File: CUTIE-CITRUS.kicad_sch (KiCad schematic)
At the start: 0 parts

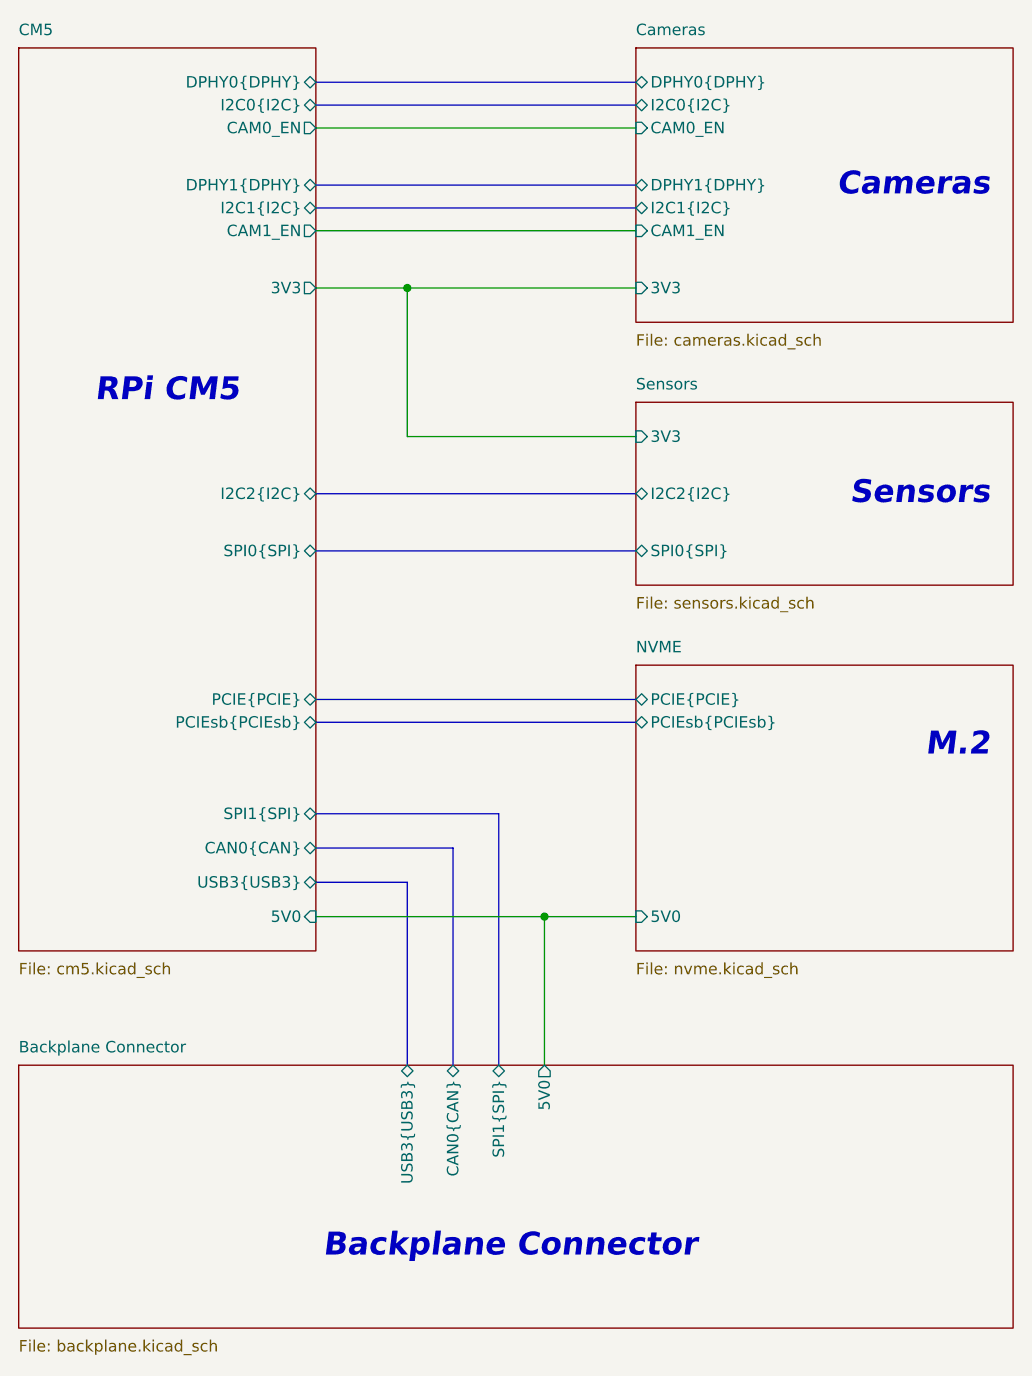
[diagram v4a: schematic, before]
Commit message: removed ublox
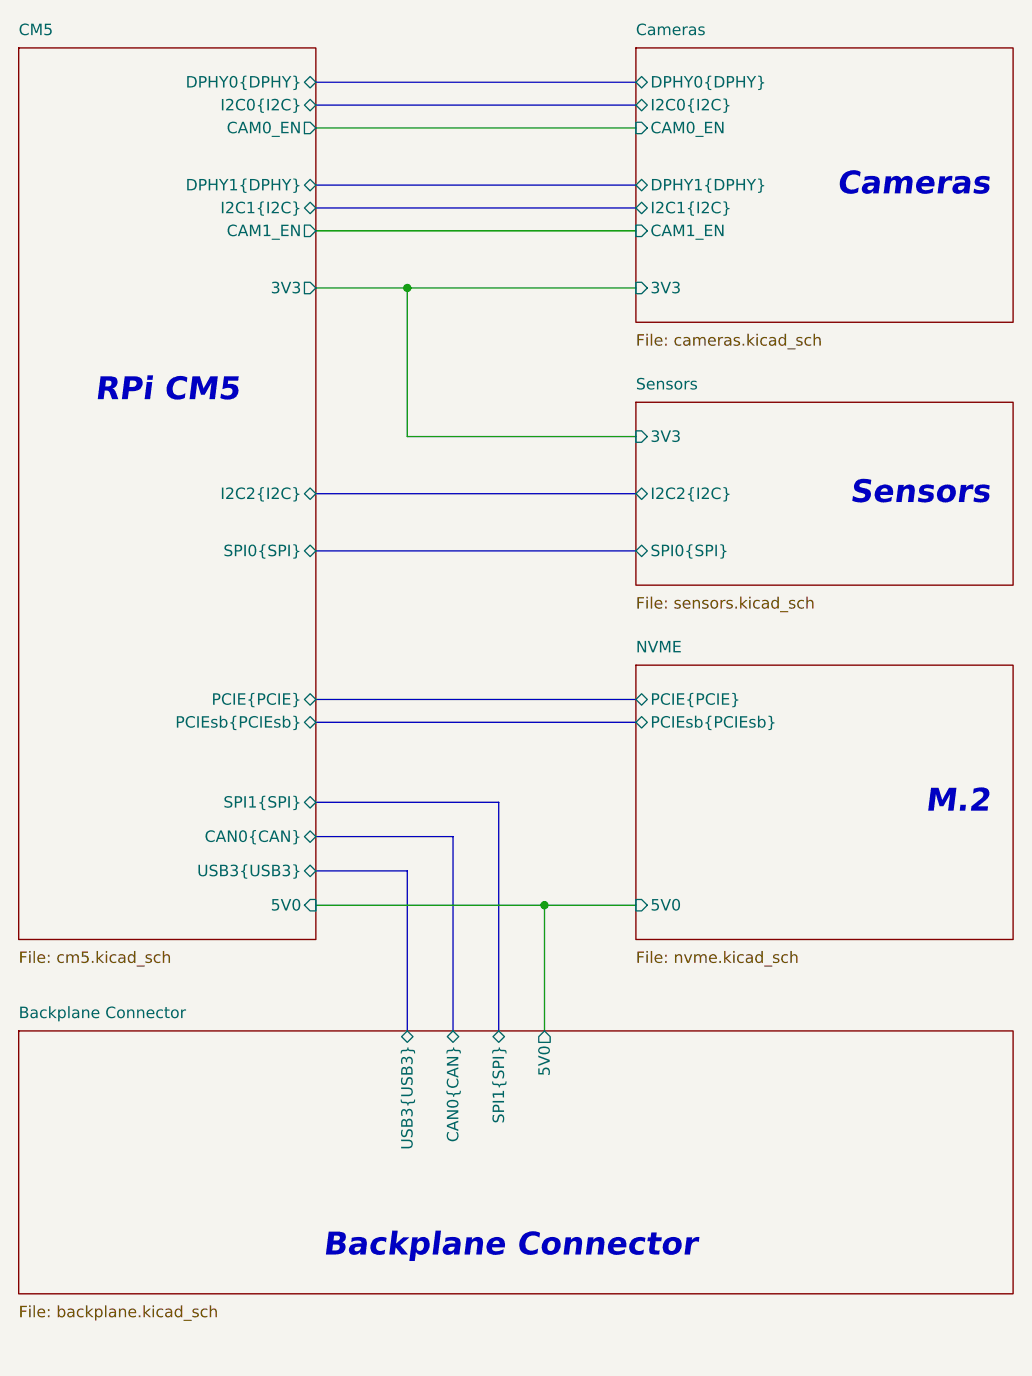
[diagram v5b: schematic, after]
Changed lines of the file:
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@@
 	(text "M.2"
 		(exclude_from_sim no)
-		(at 153.67 113.03 0)
+		(at 153.67 119.38 0)
 		(effects
 			(font
@@
 	)
 	(junction
-		(at 104.14 132.08)
+		(at 104.14 130.81)
 		(diameter 0)
 		(color 255 0 0 1)
@@
 	(wire
 		(pts
-			(xy 104.14 132.08) (xy 114.3 132.08)
+			(xy 104.14 130.81) (xy 114.3 130.81)
 		)
 		(stroke
@@
 	(bus
 		(pts
-			(xy 88.9 128.27) (xy 88.9 148.59)
-		)
-		(stroke
-			(width 0)
-			(type default)
-		)
-	)
-	(wire
-		(pts
-			(xy 104.14 132.08) (xy 104.14 148.59)
+			(xy 88.9 127) (xy 88.9 144.78)
+		)
+		(stroke
+			(width 0)
+			(type default)
+		)
+	)
+	(wire
+		(pts
+			(xy 104.14 130.81) (xy 104.14 144.78)
 		)
 		(stroke
@@
 	(bus
 		(pts
-			(xy 99.06 148.59) (xy 99.06 120.65)
+			(xy 99.06 144.78) (xy 99.06 119.38)
 		)
 		(stroke
@@
 	(bus
 		(pts
-			(xy 99.06 120.65) (xy 78.74 120.65)
+			(xy 99.06 119.38) (xy 78.74 119.38)
 		)
 		(stroke
@@
 	(wire
 		(pts
-			(xy 78.74 132.08) (xy 104.14 132.08)
+			(xy 78.74 44.45) (xy 114.3 44.45)
+		)
+		(stroke
+			(width 0)
+			(type default)
+		)
+	)
+	(wire
+		(pts
+			(xy 78.74 62.23) (xy 88.9 62.23)
+		)
+		(stroke
+			(width 0.381)
+			(type default)
+			(color 255 153 0 1)
+		)
+	)
+	(wire
+		(pts
+			(xy 88.9 62.23) (xy 114.3 62.23)
+		)
+		(stroke
+			(width 0.381)
+			(type default)
+			(color 255 153 0 1)
+		)
+	)
+	(bus
+		(pts
+			(xy 78.74 110.49) (xy 114.3 110.49)
+		)
+		(stroke
+			(width 0)
+			(type default)
+		)
+	)
+	(bus
+		(pts
+			(xy 78.74 41.91) (xy 114.3 41.91)
+		)
+		(stroke
+			(width 0)
+			(type default)
+		)
+	)
+	(bus
+		(pts
+			(xy 93.98 144.78) (xy 93.98 123.19)
+		)
+		(stroke
+			(width 0)
+			(type default)
+		)
+	)
+	(wire
+		(pts
+			(xy 78.74 55.88) (xy 114.3 55.88)
+		)
+		(stroke
+			(width 0)
+			(type default)
+		)
+	)
+	(wire
+		(pts
+			(xy 78.74 130.81) (xy 104.14 130.81)
 		)
 		(stroke
@@
 		)
 	)
-	(wire
-		(pts
-			(xy 78.74 44.45) (xy 114.3 44.45)
-		)
-		(stroke
-			(width 0)
-			(type default)
-		)
-	)
-	(wire
-		(pts
-			(xy 78.74 62.23) (xy 88.9 62.23)
+	(bus
+		(pts
+			(xy 78.74 50.8) (xy 114.3 50.8)
+		)
+		(stroke
+			(width 0)
+			(type default)
+		)
+	)
+	(wire
+		(pts
+			(xy 88.9 62.23) (xy 88.9 78.74)
 		)
 		(stroke
@@
 		)
 	)
-	(wire
-		(pts
-			(xy 88.9 62.23) (xy 114.3 62.23)
-		)
-		(stroke
-			(width 0.381)
-			(type default)
-			(color 255 153 0 1)
-		)
-	)
-	(bus
-		(pts
-			(xy 78.74 110.49) (xy 114.3 110.49)
-		)
-		(stroke
-			(width 0)
-			(type default)
-		)
-	)
-	(bus
-		(pts
-			(xy 78.74 41.91) (xy 114.3 41.91)
-		)
-		(stroke
-			(width 0)
-			(type default)
-		)
-	)
-	(bus
-		(pts
-			(xy 93.98 148.59) (xy 93.98 124.46)
-		)
-		(stroke
-			(width 0)
-			(type default)
-		)
-	)
-	(wire
-		(pts
-			(xy 78.74 55.88) (xy 114.3 55.88)
-		)
-		(stroke
-			(width 0)
-			(type default)
-		)
-	)
-	(bus
-		(pts
-			(xy 78.74 50.8) (xy 114.3 50.8)
-		)
-		(stroke
-			(width 0)
-			(type default)
-		)
-	)
-	(wire
-		(pts
-			(xy 88.9 62.23) (xy 88.9 78.74)
-		)
-		(stroke
-			(width 0.381)
-			(type default)
-			(color 255 153 0 1)
-		)
-	)
-	(bus
-		(pts
-			(xy 78.74 128.27) (xy 88.9 128.27)
-		)
-		(stroke
-			(width 0)
-			(type default)
-		)
-	)
-	(bus
-		(pts
-			(xy 93.98 124.46) (xy 78.74 124.46)
+	(bus
+		(pts
+			(xy 78.74 127) (xy 88.9 127)
+		)
+		(stroke
+			(width 0)
+			(type default)
+		)
+	)
+	(bus
+		(pts
+			(xy 93.98 123.19) (xy 78.74 123.19)
 		)
 		(stroke
@@
 	(sheet
 		(at 45.72 35.56)
-		(size 33.02 100.33)
+		(size 33.02 99.06)
 		(exclude_from_sim no)
 		(in_bom yes)
@@
 		)
 		(property "Sheetfile" "cm5.kicad_sch"
-			(at 45.72 137.16 0)
+			(at 45.72 135.89 0)
 			(effects
 				(font
@@
 		)
 		(pin "5V0" input
-			(at 78.74 132.08 0)
+			(at 78.74 130.81 0)
 			(effects
 				(font
@@
 		)
 		(pin "USB3{USB3}" bidirectional
-			(at 78.74 128.27 0)
+			(at 78.74 127 0)
 			(effects
 				(font
@@
 		)
 		(pin "SPI1{SPI}" bidirectional
-			(at 78.74 120.65 0)
+			(at 78.74 119.38 0)
 			(effects
 				(font
@@
 		)
 		(pin "CAN0{CAN}" bidirectional
-			(at 78.74 124.46 0)
+			(at 78.74 123.19 0)
 			(effects
 				(font
@@
 	(sheet
 		(at 114.3 104.14)
-		(size 41.91 31.75)
+		(size 41.91 30.48)
 		(exclude_from_sim no)
 		(in_bom yes)
@@
 		)
 		(property "Sheetfile" "nvme.kicad_sch"
-			(at 114.3 137.16 0)
+			(at 114.3 135.89 0)
 			(effects
 				(font
@@
 		)
 		(pin "5V0" input
-			(at 114.3 132.08 180)
+			(at 114.3 130.81 180)
 			(effects
 				(font
@@
 	)
 	(sheet
-		(at 45.72 148.59)
+		(at 45.72 144.78)
 		(size 110.49 29.21)
 		(exclude_from_sim no)
@@
 		)
 		(property "Sheetname" "Backplane Connector"
-			(at 45.72 147.32 0)
+			(at 45.72 143.51 0)
 			(effects
 				(font
@@
 		)
 		(property "Sheetfile" "backplane.kicad_sch"
-			(at 45.72 179.07 0)
+			(at 45.72 175.26 0)
 			(effects
 				(font
@@
 		)
 		(pin "5V0" output
-			(at 104.14 148.59 90)
+			(at 104.14 144.78 90)
 			(effects
 				(font
@@
 		)
 		(pin "USB3{USB3}" bidirectional
-			(at 88.9 148.59 90)
+			(at 88.9 144.78 90)
 			(effects
 				(font
@@
 		)
 		(pin "CAN0{CAN}" bidirectional
-			(at 93.98 148.59 90)
+			(at 93.98 144.78 90)
 			(effects
 				(font
@@
 		)
 		(pin "SPI1{SPI}" bidirectional
-			(at 99.06 148.59 90)
-			(effects
-				(font
+			(at 99.06 144.78 90)
+			(effects
+				(font

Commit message: finished defining spi/i2c gpio, CAN, off-board signals
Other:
- sheet Backplane Connector ports: added SPI2{SPI}; removed SPI1{SPI}
- sheet CM5 ports: added SPI2{SPI}; removed SPI0{SPI}
- sheet Sensors ports: added SPI1{SPI}; removed SPI0{SPI}
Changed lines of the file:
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@@
+	(bus
+		(pts
+			(xy 78.74 53.34) (xy 114.3 53.34)
+		)
+		(stroke
+			(width 0)
+			(type default)
+		)
+	)
+	(bus
+		(pts
+			(xy 78.74 39.37) (xy 114.3 39.37)
+		)
+		(stroke
+			(width 0)
+			(type default)
+		)
+	)
+	(bus
+		(pts
+			(xy 78.74 85.09) (xy 114.3 85.09)
+		)
+		(stroke
+			(width 0)
+			(type default)
+		)
+	)
+	(bus
+		(pts
+			(xy 78.74 91.44) (xy 114.3 91.44)
+		)
+		(stroke
+			(width 0)
+			(type default)
+		)
+	)
 	(bus
 		(pts
@@
 		)
 	)
-	(bus
-		(pts
-			(xy 78.74 53.34) (xy 114.3 53.34)
+	(wire
+		(pts
+			(xy 78.74 44.45) (xy 114.3 44.45)
+		)
+		(stroke
+			(width 0)
+			(type default)
+		)
+	)
+	(wire
+		(pts
+			(xy 78.74 62.23) (xy 88.9 62.23)
+		)
+		(stroke
+			(width 0.381)
+			(type default)
+			(color 255 153 0 1)
+		)
+	)
+	(wire
+		(pts
+			(xy 88.9 62.23) (xy 114.3 62.23)
+		)
+		(stroke
+			(width 0.381)
+			(type default)
+			(color 255 153 0 1)
+		)
+	)
+	(bus
+		(pts
+			(xy 78.74 110.49) (xy 114.3 110.49)
+		)
+		(stroke
+			(width 0)
+			(type default)
+		)
+	)
+	(bus
+		(pts
+			(xy 78.74 41.91) (xy 114.3 41.91)
+		)
+		(stroke
+			(width 0)
+			(type default)
+		)
+	)
+	(bus
+		(pts
+			(xy 93.98 144.78) (xy 93.98 123.19)
+		)
+		(stroke
+			(width 0)
+			(type default)
+		)
+	)
+	(wire
+		(pts
+			(xy 78.74 55.88) (xy 114.3 55.88)
 		)
 		(stroke
@@
 		(pts
 			(xy 99.06 119.38) (xy 78.74 119.38)
-		)
-		(stroke
-			(width 0)
-			(type default)
-		)
-	)
-	(bus
-		(pts
-			(xy 78.74 39.37) (xy 114.3 39.37)
-		)
-		(stroke
-			(width 0)
-			(type default)
-		)
-	)
-	(bus
-		(pts
-			(xy 78.74 85.09) (xy 114.3 85.09)
-		)
-		(stroke
-			(width 0)
-			(type default)
-		)
-	)
-	(bus
-		(pts
-			(xy 78.74 91.44) (xy 114.3 91.44)
-		)
-		(stroke
-			(width 0)
-			(type default)
-		)
-	)
-	(wire
-		(pts
-			(xy 78.74 44.45) (xy 114.3 44.45)
-		)
-		(stroke
-			(width 0)
-			(type default)
-		)
-	)
-	(wire
-		(pts
-			(xy 78.74 62.23) (xy 88.9 62.23)
-		)
-		(stroke
-			(width 0.381)
-			(type default)
-			(color 255 153 0 1)
-		)
-	)
-	(wire
-		(pts
-			(xy 88.9 62.23) (xy 114.3 62.23)
-		)
-		(stroke
-			(width 0.381)
-			(type default)
-			(color 255 153 0 1)
-		)
-	)
-	(bus
-		(pts
-			(xy 78.74 110.49) (xy 114.3 110.49)
-		)
-		(stroke
-			(width 0)
-			(type default)
-		)
-	)
-	(bus
-		(pts
-			(xy 78.74 41.91) (xy 114.3 41.91)
-		)
-		(stroke
-			(width 0)
-			(type default)
-		)
-	)
-	(bus
-		(pts
-			(xy 93.98 144.78) (xy 93.98 123.19)
-		)
-		(stroke
-			(width 0)
-			(type default)
-		)
-	)
-	(wire
-		(pts
-			(xy 78.74 55.88) (xy 114.3 55.88)
 		)
 		(stroke
@@
 			)
 		)
-		(pin "SPI0{SPI}" bidirectional
-			(at 78.74 91.44 0)
-			(effects
-				(font
-					(size 1.27 1.27)
-				)
-				(justify right)
-			)
-		)
 		(pin "I2C0{I2C}" bidirectional
 			(at 78.74 41.91 0)
@@
 			)
 		)
-		(pin "SPI1{SPI}" bidirectional
-			(at 78.74 119.38 0)
-			(effects
-				(font
-					(size 1.27 1.27)
-				)
-				(justify right)
-			)
-		)
 		(pin "CAN0{CAN}" bidirectional
 			(at 78.74 123.19 0)
+			(effects
+				(font
+					(size 1.27 1.27)
+				)
+				(justify right)
+			)
+		)
+		(pin "SPI1{SPI}" bidirectional
+			(at 78.74 91.44 0)
+			(effects
+				(font
+					(size 1.27 1.27)
+				)
+				(justify right)
+			)
+		)
+		(pin "SPI2{SPI}" bidirectional
+			(at 78.74 119.38 0)
 			(effects
 				(font
@@
 			)
 		)
-		(pin "SPI0{SPI}" bidirectional
-			(at 114.3 91.44 180)
-			(effects
-				(font
-					(size 1.27 1.27)
-				)
-				(justify left)
-			)
-		)
 		(pin "I2C2{I2C}" bidirectional
 			(at 114.3 85.09 180)
+			(effects
+				(font
+					(size 1.27 1.27)
+				)
+				(justify left)
+			)
+		)
+		(pin "SPI1{SPI}" bidirectional
+			(at 114.3 91.44 180)
 			(effects
 				(font
@@
 			)
 		)
-		(pin "SPI1{SPI}" bidirectional
+		(pin "SPI2{SPI}" bidirectional
 			(at 99.06 144.78 90)
 			(effects
